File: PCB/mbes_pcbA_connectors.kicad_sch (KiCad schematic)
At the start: 43 parts, among them K1 HK19F-DCxxV-SHC, Q2 BC817, Q22 BC807, Q24 BC807, Q3 TPCA8120,L1Q, Q4 BC817, U2 L7805

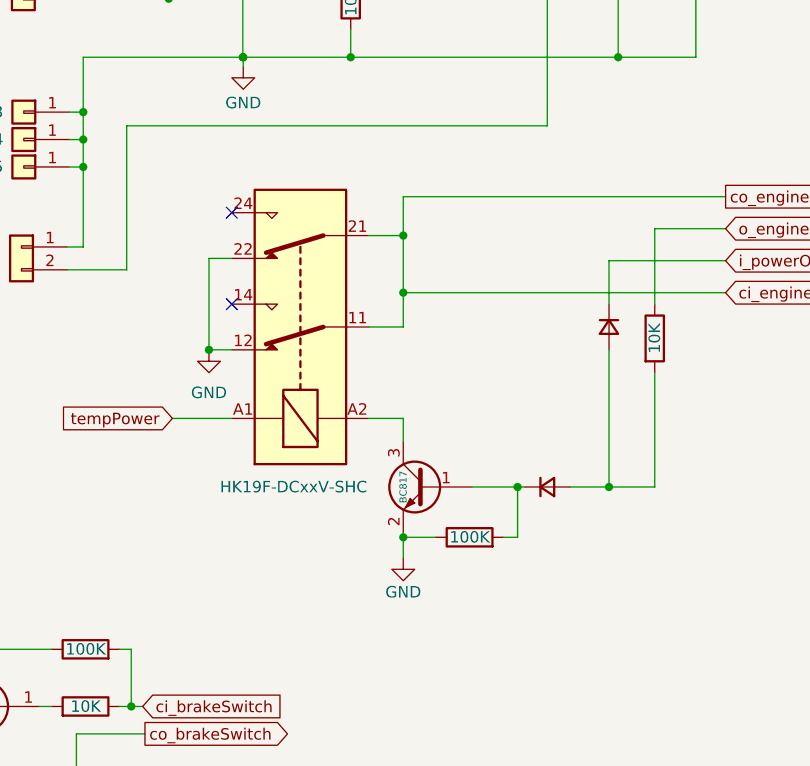
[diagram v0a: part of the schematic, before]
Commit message: Fly back diode added to relay
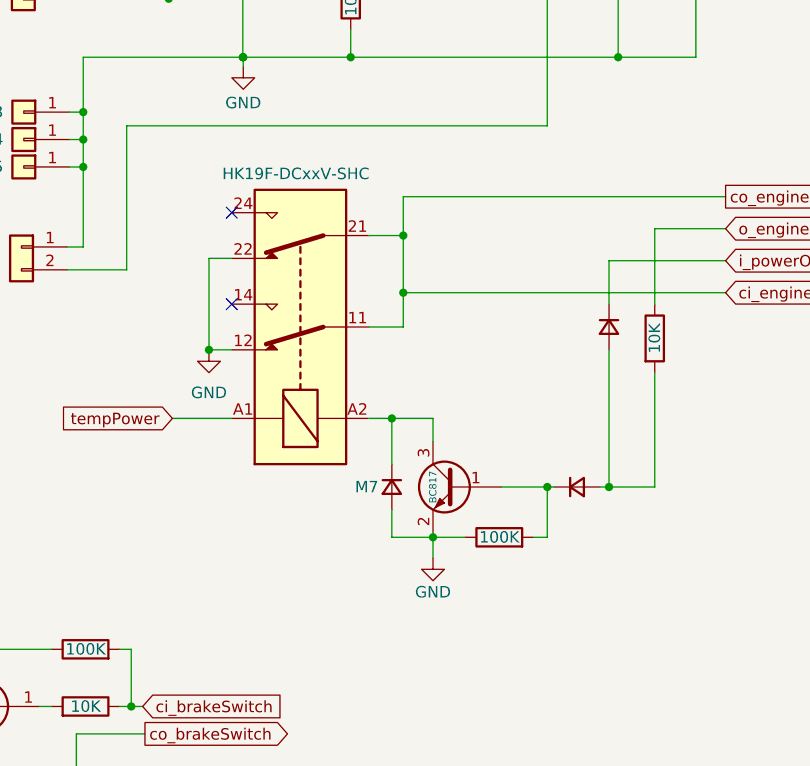
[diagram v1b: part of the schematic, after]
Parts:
- added flyback-1: M7, Diode_SMD:D_2114_3652Metric_Pad1.85x3.75mm_HandSolder, symbol Device:D_Small
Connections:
- net GND: now also flyback-1.2 (A)
- net at K1.A2, Q4.3 (C): now also flyback-1.1 (K)
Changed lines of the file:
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@@
 	)
 	(junction
+		(at 178.562 125.984)
+		(diameter 0)
+		(color 0 0 0 0)
+	)
+	(junction
 		(at 86.868 163.068)
 		(diameter 0)
@@
 	)
 	(junction
-		(at 192.532 133.604)
+		(at 195.834 133.604)
 		(diameter 0)
 		(color 0 0 0 0)
@@
 	)
 	(junction
-		(at 179.832 139.192)
+		(at 183.134 139.192)
 		(diameter 0)
 		(color 0 0 0 0)
@@
 	(wire
 		(pts
+			(xy 178.562 125.984) (xy 178.562 131.064)
+		)
+		(stroke
+			(width 0)
+			(type default)
+		)
+	)
+	(wire
+		(pts
 			(xy 85.6996 42.2656) (xy 73.8124 42.2656)
 		)
@@
 	(wire
 		(pts
-			(xy 179.832 139.192) (xy 179.832 141.478)
+			(xy 183.134 139.192) (xy 183.134 141.478)
 		)
 		(stroke
@@
 	(wire
 		(pts
-			(xy 176.022 125.984) (xy 179.832 125.984)
+			(xy 176.022 125.984) (xy 178.562 125.984)
 		)
 		(stroke
@@
 	(wire
 		(pts
-			(xy 179.832 139.192) (xy 183.388 139.192)
+			(xy 183.134 139.192) (xy 186.69 139.192)
 		)
 		(stroke
@@
 	(wire
 		(pts
-			(xy 198.374 133.604) (xy 202.692 133.604)
+			(xy 201.676 133.604) (xy 202.692 133.604)
 		)
 		(stroke
@@
 	(wire
 		(pts
-			(xy 179.832 125.984) (xy 179.832 128.524)
+			(xy 183.134 125.984) (xy 183.134 128.524)
 		)
 		(stroke
@@
 	(wire
 		(pts
-			(xy 191.008 139.192) (xy 192.532 139.192)
+			(xy 194.31 139.192) (xy 195.834 139.192)
 		)
 		(stroke
@@
 	(wire
 		(pts
+			(xy 178.562 139.192) (xy 183.134 139.192)
+		)
+		(stroke
+			(width 0)
+			(type default)
+		)
+	)
+	(wire
+		(pts
 			(xy 69.723 76.962) (xy 69.723 73.279)
 		)
@@
 	(wire
 		(pts
-			(xy 192.532 133.604) (xy 193.294 133.604)
+			(xy 195.834 133.604) (xy 196.596 133.604)
 		)
 		(stroke
@@
 	(wire
 		(pts
+			(xy 178.562 125.984) (xy 183.134 125.984)
+		)
+		(stroke
+			(width 0)
+			(type default)
+		)
+	)
+	(wire
+		(pts
 			(xy 195.834 32.512) (xy 195.834 35.052)
 		)
@@
 	(wire
 		(pts
-			(xy 192.532 139.192) (xy 192.532 133.604)
+			(xy 195.834 139.192) (xy 195.834 133.604)
 		)
 		(stroke
@@
 	(wire
 		(pts
-			(xy 179.832 139.192) (xy 179.832 138.684)
+			(xy 183.134 139.192) (xy 183.134 138.684)
 		)
 		(stroke
@@
 	(wire
 		(pts
+			(xy 178.562 136.144) (xy 178.562 139.192)
+		)
+		(stroke
+			(width 0)
+			(type default)
+		)
+	)
+	(wire
+		(pts
 			(xy 85.598 39.116) (xy 76.708 39.116)
 		)
@@
 	(wire
 		(pts
-			(xy 187.452 133.604) (xy 192.532 133.604)
+			(xy 190.754 133.604) (xy 195.834 133.604)
 		)
 		(stroke
@@
 	(symbol
 		(lib_id "Transistor_BJT:BC817")
-		(at 182.372 133.604 0)
+		(at 185.674 133.604 0)
 		(mirror y)
 		(unit 1)
@@
 		(dnp no)
 		(property "Reference" "Q4"
-			(at 175.3616 133.604 90)
+			(at 178.6636 133.604 90)
 			(effects
 				(font
@@
 		)
 		(property "Value" "BC817"
-			(at 179.832 133.604 90)
+			(at 183.134 133.604 90)
 			(effects
 				(font
@@
 		)
 		(property "Footprint" "Package_TO_SOT_SMD:SOT-23"
-			(at 177.292 135.509 0)
+			(at 180.594 135.509 0)
 			(effects
 				(font
@@
 		)
 		(property "Datasheet" "https://www.onsemi.com/pub/Collateral/BC818-D.pdf"
-			(at 182.372 133.604 0)
+			(at 185.674 133.604 0)
 			(effects
 				(font
@@
 		)
 		(property "Description" ""
-			(at 182.372 133.604 0)
+			(at 185.674 133.604 0)
 			(effects
 				(font
@@
 	(symbol
 		(lib_id "Device:R")
-		(at 187.198 139.192 90)
+		(at 190.5 139.192 90)
 		(unit 1)
 		(exclude_from_sim no)
@@
 		(dnp no)
 		(property "Reference" "RA1"
-			(at 187.198 145.542 90)
+			(at 190.5 145.542 90)
 			(effects
 				(font
@@
 		)
 		(property "Value" "100K"
-			(at 187.198 139.192 90)
+			(at 190.5 139.192 90)
 			(effects
 				(font
@@
 		)
 		(property "Footprint" "Resistor_SMD:R_1206_3216Metric"
-			(at 187.198 140.97 90)
+			(at 190.5 140.97 90)
 			(effects
 				(font
@@
 		)
 		(property "Datasheet" "~"
-			(at 187.198 139.192 0)
+			(at 190.5 139.192 0)
 			(effects
 				(font
@@
 		)
 		(property "Description" ""
-			(at 187.198 139.192 0)
+			(at 190.5 139.192 0)
 			(effects
 				(font
@@
 	)
 	(symbol
+		(lib_id "Device:D_Small")
+		(at 178.562 133.604 270)
+		(unit 1)
+		(exclude_from_sim no)
+		(in_bom yes)
+		(on_board yes)
+		(dnp no)
+		(property "Reference" "flyback-1"
+			(at 184.4548 133.604 0)
+			(effects
+				(font
+					(size 1.27 1.27)
+				)
+				(hide yes)
+			)
+		)
+		(property "Value" "M7"
+			(at 175.768 133.604 90)
+			(effects
+				(font
+					(size 1.27 1.27)
+				)
+			)
+		)
+		(property "Footprint" "Diode_SMD:D_2114_3652Metric_Pad1.85x3.75mm_HandSolder"
+			(at 178.562 133.604 90)
+			(effects
+				(font
+					(size 1.27 1.27)
+				)
+				(hide yes)
+			)
+		)
+		(property "Datasheet" "~"
+			(at 178.562 133.604 90)
+			(effects
+				(font
+					(size 1.27 1.27)
+				)
+				(hide yes)
+			)
+		)
+		(property "Description" ""
+			(at 178.562 133.604 0)
+			(effects
+				(font
+					(size 1.27 1.27)
+				)
+				(hide yes)
+			)
+		)
+		(property "Sim.Device" "D"
+			(at 178.562 133.604 0)
+			(effects
+				(font
+					(size 1.27 1.27)
+				)
+				(hide yes)
+			)
+		)
+		(property "Sim.Pins" "1=K 2=A"
+			(at 178.562 133.604 0)
+			(effects
+				(font
+					(size 1.27 1.27)
+				)
+				(hide yes)
+			)
+		)
+		(pin "1"
+		)
+		(pin "2"
+		)
+		(instances
+			(project "main"
+				(path "/709d0967-afe5-49d3-92a5-d2bb94550bdb/3216a3d3-5416-4017-b51b-dad2d5be039c"
+					(reference "flyback-1")
+					(unit 1)
+				)
+			)
+		)
+	)
+	(symbol
 		(lib_id "Connector_Generic:Conn_01x02")
 		(at 137.7188 67.5132 0)
@@
 		)
 		(property "Value" "HK19F-DCxxV-SHC"
-			(at 167.64 133.604 90)
+			(at 167.894 98.806 90)
 			(effects
 				(font
@@
 	(symbol
 		(lib_id "power:GND")
-		(at 179.832 141.478 0)
+		(at 183.134 141.478 0)
 		(unit 1)
 		(exclude_from_sim no)
@@
 		(dnp no)
 		(property "Reference" "#PWR010"
-			(at 179.832 147.828 0)
+			(at 183.134 147.828 0)
 			(effects
 				(font
@@
 		)
 		(property "Value" "GND"
-			(at 179.832 145.288 0)
+			(at 183.134 145.288 0)
 			(effects
 				(font
@@
 		)
 		(property "Footprint" ""
-			(at 179.832 141.478 0)
+			(at 183.134 141.478 0)
 			(effects
 				(font
@@
 		)
 		(property "Datasheet" ""
-			(at 179.832 141.478 0)
+			(at 183.134 141.478 0)
 			(effects
 				(font
@@
 		)
 		(property "Description" ""
-			(at 179.832 141.478 0)
+			(at 183.134 141.478 0)
 			(effects
 				(font
@@
 	(symbol
 		(lib_id "Device:D_Small")
-		(at 195.834 133.604 0)
+		(at 199.136 133.604 0)
 		(unit 1)
 		(exclude_from_sim no)
@@
 		(fields_autoplaced yes)
 		(property "Reference" "D2"
-			(at 195.834 127.7112 0)
+			(at 199.136 127.7112 0)
 			(effects
 				(font
@@
 		)
 		(property "Value" "D_Small"
-			(at 195.834 130.2512 0)
+			(at 199.136 130.2512 0)
 			(effects
 				(font
@@
 		)
 		(property "Footprint" "Diode_SMD:D_1210_3225Metric_Pad1.42x2.65mm_HandSolder"
-			(at 195.834 133.604 90)
+			(at 199.136 133.604 90)
 			(effects
 				(font
@@
 		)
 		(property "Datasheet" "~"
-			(at 195.834 133.604 90)
+			(at 199.136 133.604 90)
 			(effects
 				(font
@@
 		)
 		(property "Description" ""
-			(at 195.834 133.604 0)
+			(at 199.136 133.604 0)
 			(effects
 				(font
@@
 		)
 		(property "Sim.Device" "D"
-			(at 195.834 133.604 0)
+			(at 199.136 133.604 0)
 			(effects
 				(font
@@
 		)
 		(property "Sim.Pins" "1=K 2=A"
-			(at 195.834 133.604 0)
+			(at 199.136 133.604 0)
 			(effects
 				(font

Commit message: Merge from ESP32__dualPCB
- Wrong diode footprints fixed
- Floating FET's source pin fixed
- Unuseful horn's propagation fixed
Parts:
- D1, D2, D3: value D_Small -> PMEG40T30ER; footprint Diode_SMD:D_1210_3225Metric_Pad1.42x2.65mm_HandSolder -> Diode_SMD:Nexperia_CFP3_SOD-123W
- flyback-1: value M7 -> PMEG40T30ER; footprint Diode_SMD:D_2114_3652Metric_Pad1.85x3.75mm_HandSolder -> Diode_SMD:Nexperia_CFP3_SOD-123W
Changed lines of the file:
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@@
 			)
 		)
-		(property "Value" "D_Small"
+		(property "Value" "PMEG40T30ER"
 			(at 206.0448 115.824 0)
 			(effects
@@
 			)
 		)
-		(property "Footprint" "Diode_SMD:D_1210_3225Metric_Pad1.42x2.65mm_HandSolder"
+		(property "Footprint" "Diode_SMD:Nexperia_CFP3_SOD-123W"
 			(at 202.692 115.824 90)
 			(effects
@@
 			)
 		)
-		(property "Value" "M7"
+		(property "Value" "PMEG40T30ER"
 			(at 175.768 133.604 90)
 			(effects
@@
 					(size 1.27 1.27)
 				)
-			)
-		)
-		(property "Footprint" "Diode_SMD:D_2114_3652Metric_Pad1.85x3.75mm_HandSolder"
+				(hide yes)
+			)
+		)
+		(property "Footprint" "Diode_SMD:Nexperia_CFP3_SOD-123W"
 			(at 178.562 133.604 90)
 			(effects
@@
 			)
 		)
-		(property "Value" "D_Small"
+		(property "Value" "PMEG40T30ER"
 			(at 170.434 59.1312 0)
 			(effects
@@
 			)
 		)
-		(property "Footprint" "Diode_SMD:D_1210_3225Metric_Pad1.42x2.65mm_HandSolder"
+		(property "Footprint" "Diode_SMD:Nexperia_CFP3_SOD-123W"
 			(at 170.434 62.484 90)
 			(effects
@@
 			)
 		)
-		(property "Value" "D_Small"
+		(property "Value" "PMEG40T30ER"
 			(at 199.136 130.2512 0)
 			(effects
@@
 			)
 		)
-		(property "Footprint" "Diode_SMD:D_1210_3225Metric_Pad1.42x2.65mm_HandSolder"
+		(property "Footprint" "Diode_SMD:Nexperia_CFP3_SOD-123W"
 			(at 199.136 133.604 90)
 			(effects
